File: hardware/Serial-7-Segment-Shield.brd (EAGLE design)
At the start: 59.7 x 53.3 mm, 28 parts, among them U1 ARDUINO_SHIELDLABEL

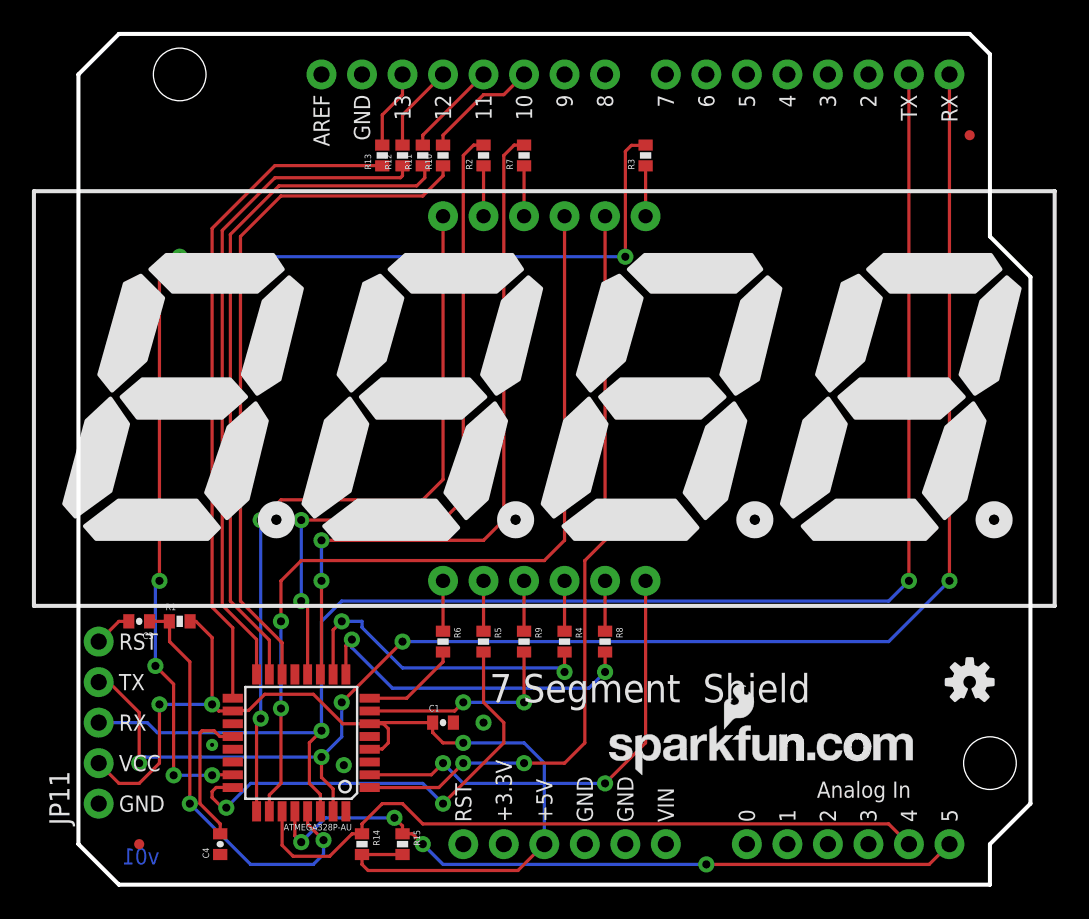
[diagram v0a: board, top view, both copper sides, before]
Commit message: Updated hardware to v02.
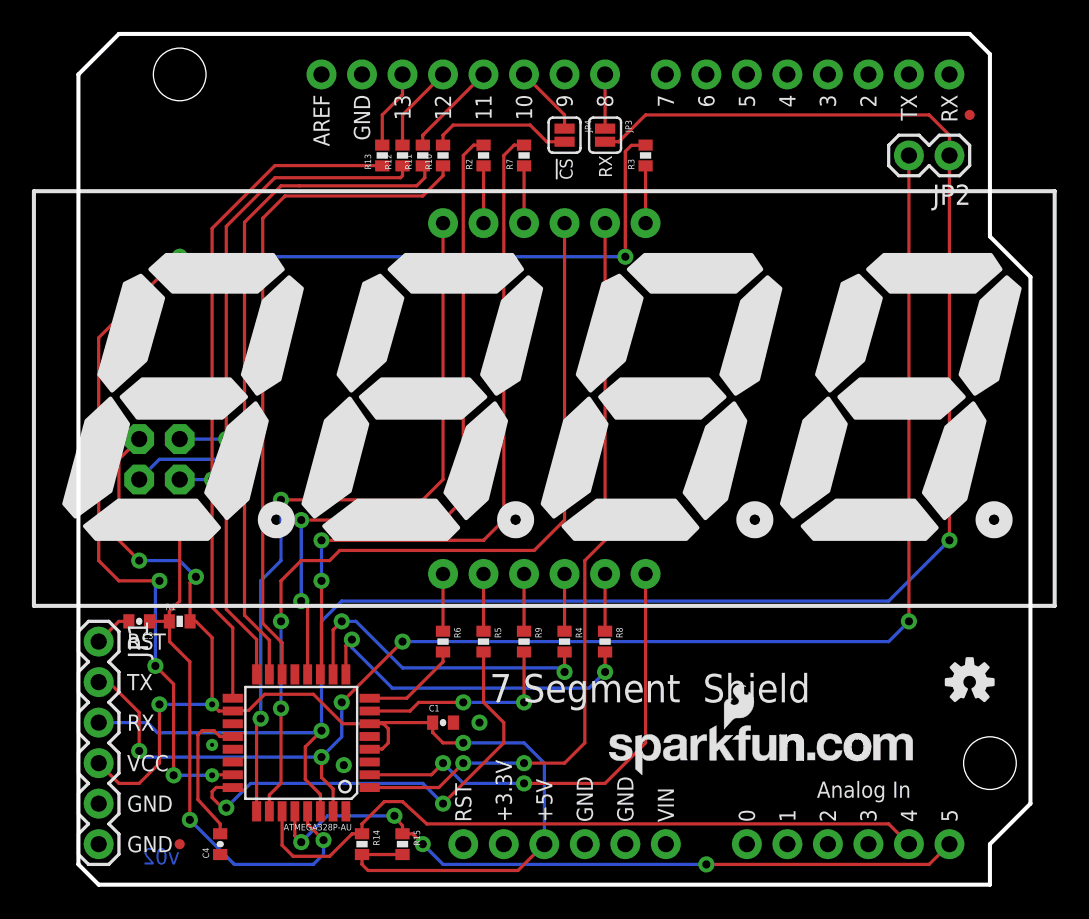
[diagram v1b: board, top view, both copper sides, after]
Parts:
- removed JP11: (no value), SparkFun-Connectors:1X05_NO_SILK
- added J1: AVR_SPI_PRG_6PTH, SparkFun-Connectors:2X3
- added JP1: (no value), SparkFun-Connectors:1X06
- added JP2: (no value), SparkFun-Connectors:1X02
- added JP3, JP4: NC, SparkFun-Passives:SJ_2S
- R2, R3, R4, R5, R6, R7, R8, R9: value 1k -> 100
- moved JP10 2.54 mm to (6.35, 2.54)
- moved JP9 1.27 mm to (55.9, 48.3)
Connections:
- new net N$6: JP4.1, U1.D10
- new net N$7: JP3.1, U1.D8
- net GND: now also J1.6, JP1.5, JP1.6; no longer JP11.1
- net MISO: now also J1.1
- net MOSI: now also J1.4
- net N$13: now also JP1.1; no longer JP11.5
- net N$5: now also JP4.2; no longer U1.D10
- net RESET: now also J1.5
- net RX: now also JP1.3, JP2.1, JP3.2; no longer JP11.3, U1.TX
- net SCK: now also J1.3
- net TX: now also JP1.2, JP2.2; no longer JP11.4, U1.RX
- net VCC: now also J1.2, JP1.4; no longer JP11.2
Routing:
- net RX: track 96.4 -> 116.7 mm
- net VCC: track 65.5 -> 81.1 mm, vias 3 -> 5
- net RESET: track 26.5 -> 33.7 mm
- net TX: track 98.8 -> 91.9 mm
- net MOSI: track 43.1 -> 49.4 mm, vias 0 -> 1
- net B: track 73.3 -> 78.0 mm
- net N$6: track 0.00 -> 4.45 mm
- net N$7: track 0.00 -> 3.40 mm
- net MISO: track 42.1 -> 44.8 mm, vias 0 -> 1
- net SCK: track 42.3 -> 44.3 mm, vias 0 -> 1
- net N$5: track 7.28 -> 8.94 mm
- net !SS: track 43.4 -> 42.1 mm
- net DIG2: track 53.9 -> 52.7 mm
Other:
- outline, holes or cut-outs redrawn
- board text added: "!CS"
- board text added: "v02"
- board text removed: "v01"

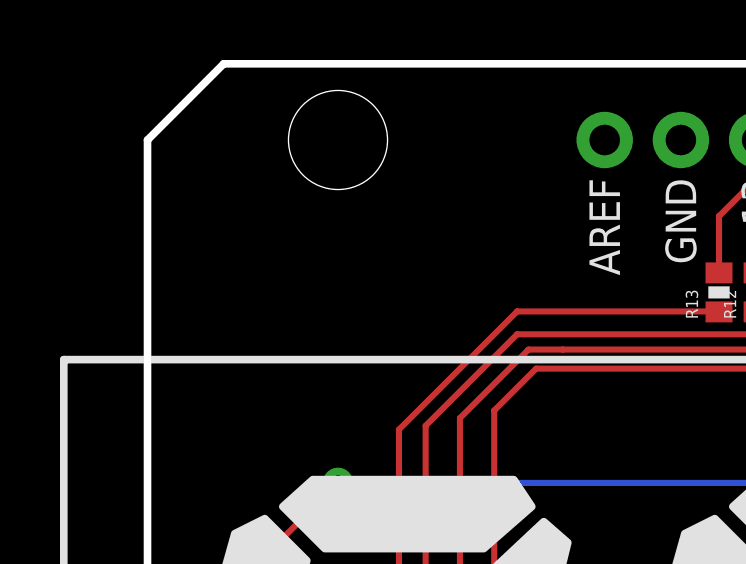
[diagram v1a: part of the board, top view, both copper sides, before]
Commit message: Minor update to v02, now includes color selection silk.
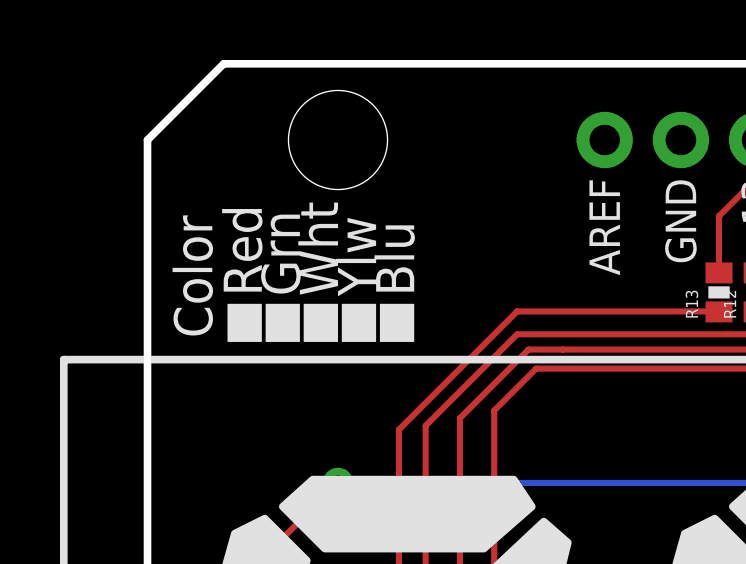
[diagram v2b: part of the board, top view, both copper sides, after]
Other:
- board text added: "Blu"
- board text added: "Color"
- board text added: "Grn"
- board text added: "Red"
- board text added: "Wht"
- board text added: "Ylw"
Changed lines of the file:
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@@
 <text x="3.048" y="4.572" size="1.016" layer="21" font="vector" ratio="15">GND</text>
 <text x="6.35" y="1.27" size="1.016" layer="16" font="vector" ratio="15" rot="MR0">v02</text>
-<text x="36.83" y="-17.78" size="1.778" layer="104" font="vector" ratio="15">Jordan McConnell</text>
+<text x="36.83" y="-17.78" size="1.778" layer="27" font="vector" ratio="15">Jordan McConnell</text>
 <text x="3.048" y="2.032" size="1.016" layer="21" font="vector" ratio="15">GND</text>
 <text x="32.639" y="45.72" size="0.8128" layer="21" font="vector" ratio="15" rot="R270">RX</text>
 <text x="30.988" y="44.196" size="0.8128" layer="21" font="vector" ratio="15" rot="R90">!CS</text>
+<text x="2.159" y="44.196" size="1.27" layer="21" font="vector" ratio="15" rot="R90">Color</text>
+<text x="3.81" y="45.593" size="1.27" layer="21" font="vector" ratio="15" rot="R90">Red</text>
+<text x="5.08" y="45.593" size="1.27" layer="21" font="vector" ratio="15" rot="R90">Grn</text>
+<text x="6.35" y="45.593" size="1.27" layer="21" font="vector" ratio="15" rot="R90">Wht</text>
+<text x="7.62" y="45.593" size="1.27" layer="21" font="vector" ratio="15" rot="R90">Ylw</text>
+<text x="8.89" y="45.593" size="1.27" layer="21" font="vector" ratio="15" rot="R90">Blu</text>
+<rectangle x1="2.6035" y1="44.1325" x2="3.8735" y2="45.2755" layer="21" rot="R90"/>
+<rectangle x1="3.8735" y1="44.1325" x2="5.1435" y2="45.2755" layer="21" rot="R90"/>
+<rectangle x1="5.1435" y1="44.1325" x2="6.4135" y2="45.2755" layer="21" rot="R90"/>
+<rectangle x1="6.4135" y1="44.1325" x2="7.6835" y2="45.2755" layer="21" rot="R90"/>
+<rectangle x1="7.6835" y1="44.1325" x2="8.9535" y2="45.2755" layer="21" rot="R90"/>
 </plain>
 <attributes>
@@
 </signal>
 </signals>
-<errors>
-</errors>
 </board>
 </drawing>
